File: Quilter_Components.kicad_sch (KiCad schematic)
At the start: 43 parts, among them J1 Conn_01x10_Male, J2 Conn_01x10_Male, J3 Conn_01x10_Male, J4 Eurorack_10_pin_power, U1 TL072, U2 TL074, U3 TL074, U4 TL074

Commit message: Added Readme and revision notes
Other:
- note added: "Potential V2 fixes: Mixed audio too loud - R6 try 4.7k in place of 10k (or variable resistor) Mixed audio has DC offset - use blocking caps on Audio_Out? Resonance cannot reach maximum on all variants - reduce Q Control resistor from 27k to 24-25k (R27, R40, R53, R66)"
- company: (none) -> Mountjoy Modular
- title: (none) -> Quilter Components
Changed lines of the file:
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@@
 (kicad_sch (version 20211123) (generator eeschema)
   (paper "A4")
+  (title_block
+    (title "Quilter Components")
+    (date "2023-03-22")
+    (rev "v1.0")
+    (company "Mountjoy Modular")
+  )
   (junction (at 66.04 167.64) (diameter 0) (color 0 0 0 0)
   )
@@
     (effects (font (size 3 3) (thickness 0.6) bold) (justify left bottom))
   )
+  (text "Potential V2 fixes:\nMixed audio too loud - R6 try 4.7k in place of 10k (or variable resistor)\nMixed audio has DC offset - use blocking caps on Audio_Out?\nResonance cannot reach maximum on all variants\n - reduce Q Control resistor from 27k to 24-25k (R27, R40, R53, R66)"
+    (at 204.47 179.07 0)
+    (effects (font (size 1.27 1.27)) (justify left bottom))
+  )
   (text "Interconnects and Test Points" (at 15.24 128.27 0)

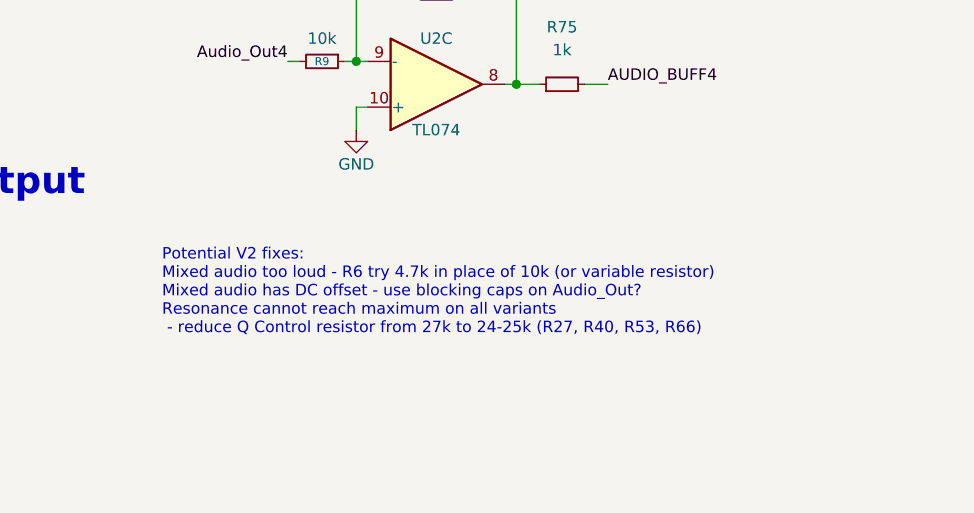
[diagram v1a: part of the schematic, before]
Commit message: Started adding DC blocking caps to audio outputs
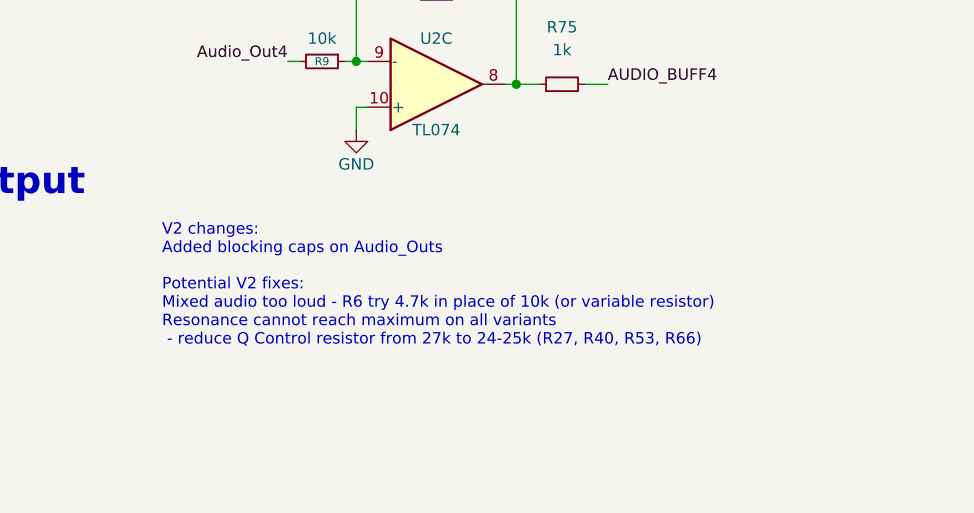
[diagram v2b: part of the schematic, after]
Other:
- note added: "Potential V2 fixes: Mixed audio too loud - R6 try 4.7k in place of 10k (or variable resistor) Resonance cannot reach maximum on all variants - reduce Q Control resistor from 27k to 24-25k (R27, R40, R53, R66)"
- note added: "V2 changes: Added blocking caps on Audio_Outs"
- note removed: "Potential V2 fixes: Mixed audio too loud - R6 try 4.7k in place of 10k (or variable resistor) Mixed audio has DC offset - use blocking caps on Audio_Out? Resonance cannot reach maximum on all variants - reduce Q Control resistor from 27k to 24-25k (R27, R40, R53, R66)"
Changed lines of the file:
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@@
     (effects (font (size 3 3) (thickness 0.6) bold) (justify left bottom))
+  )
+  (text "V2 changes:\nAdded blocking caps on Audio_Outs\n" (at 204.47 170.18 0)
+    (effects (font (size 1.27 1.27)) (justify left bottom))
   )
   (text "Output" (at 179.705 163.83 0)
     (effects (font (size 3 3) (thickness 0.6) bold) (justify left bottom))
   )
-  (text "Potential V2 fixes:\nMixed audio too loud - R6 try 4.7k in place of 10k (or variable resistor)\nMixed audio has DC offset - use blocking caps on Audio_Out?\nResonance cannot reach maximum on all variants\n - reduce Q Control resistor from 27k to 24-25k (R27, R40, R53, R66)"
-    (at 204.47 179.07 0)
+  (text "Potential V2 fixes:\nMixed audio too loud - R6 try 4.7k in place of 10k (or variable resistor)\nResonance cannot reach maximum on all variants\n - reduce Q Control resistor from 27k to 24-25k (R27, R40, R53, R66)"
+    (at 204.47 180.34 0)
     (effects (font (size 1.27 1.27)) (justify left bottom))
   )
@@
       (reference "C46") (unit 1) (value "1uF") (footprint "Capacitor_SMD:C_0603_1608Metric_Pad1.08x0.95mm_HandSolder")
     )
+    (path "/e84f8fd9-bd0a-4839-99bd-bd22e1164470/2c05cbd3-ef67-48b3-ba85-a3bd09df8735"
+      (reference "C47") (unit 1) (value "10uF") (footprint "Capacitor_SMD:C_0603_1608Metric_Pad1.08x0.95mm_HandSolder")
+    )
+    (path "/d9279b8b-eddd-468d-889c-ab682c020f45/2c05cbd3-ef67-48b3-ba85-a3bd09df8735"
+      (reference "C48") (unit 1) (value "10uF") (footprint "Capacitor_SMD:C_0603_1608Metric_Pad1.08x0.95mm_HandSolder")
+    )
+    (path "/3b233311-750f-4948-b3ee-a90810d15ca2/2c05cbd3-ef67-48b3-ba85-a3bd09df8735"
+      (reference "C49") (unit 1) (value "10uF") (footprint "Capacitor_SMD:C_0603_1608Metric_Pad1.08x0.95mm_HandSolder")
+    )
+    (path "/4ed2cc61-9552-41b0-be0f-c23455f3fe4c/2c05cbd3-ef67-48b3-ba85-a3bd09df8735"
+      (reference "C50") (unit 1) (value "10uF") (footprint "Capacitor_SMD:C_0603_1608Metric_Pad1.08x0.95mm_HandSolder")
+    )
     (path "/37b546d9-67b1-4476-930d-e62983801a78"

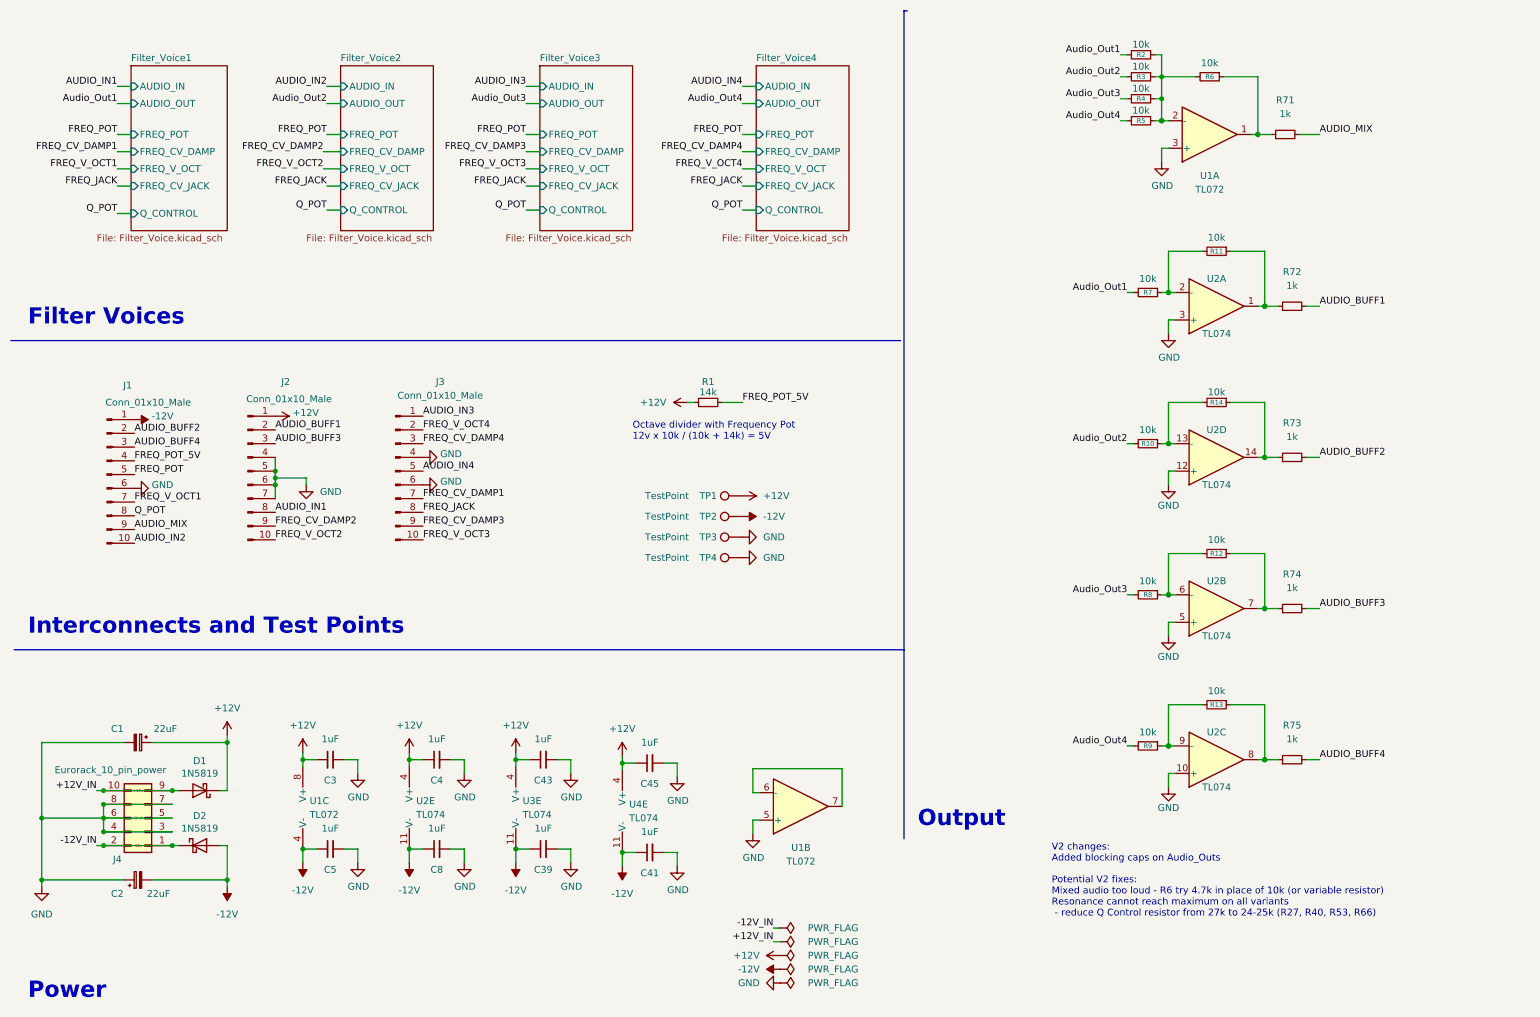
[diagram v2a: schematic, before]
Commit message: Updates for v2, including dc blocking caps on output
Also adjusted lower range of cutoff knob and tweaked various resistor values
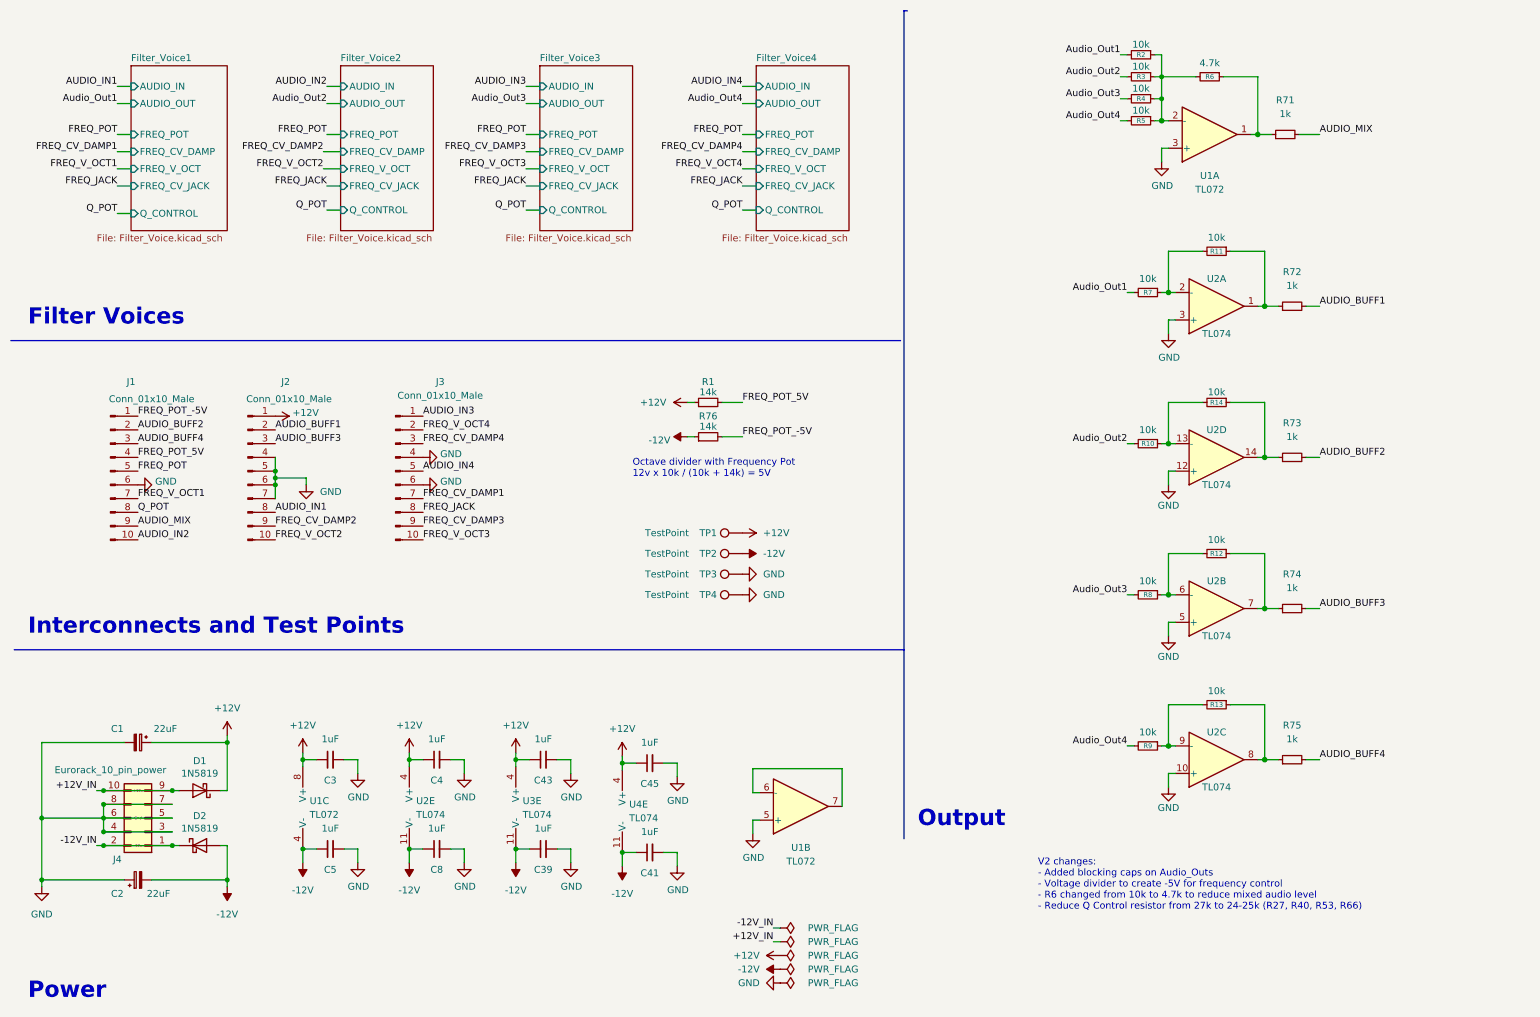
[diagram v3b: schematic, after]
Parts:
- added R76: 14k, Resistor_SMD:R_0603_1608Metric_Pad0.98x0.95mm_HandSolder, symbol Device:R_Small
- R6: value 10k -> 4.7k
- TP1, TP2, TP3, TP4: now left out of the parts list
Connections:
- net -12V: now also R76.1; no longer J1.1 (Pin_1)
- new net FREQ_POT_-5V: J1.1 (Pin_1), R76.2
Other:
- note added: "V2 changes: - Added blocking caps on Audio_Outs - Voltage divider to create -5V for frequency control - R6 changed from 10k to 4.7k to reduce mixed audio level - Reduce Q Control resistor from 27k to 24-25k (R27, R40, R53, R66)"
- note removed: "Potential V2 fixes: Mixed audio too loud - R6 try 4.7k in place of 10k (or variable resistor) Resonance cannot reach maximum on all variants - reduce Q Control resistor from 27k to 24-25k (R27, R40, R53, R66)"
- note removed: "V2 changes: Added blocking caps on Audio_Outs"
- moved on the sheet: J1, TP1, TP2, TP3, TP4

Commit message: Prepared v2 Controls and Components for manufacture
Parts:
- C1: Part_Number C134798 -> (none); Rotation 360 -> (none)
- C2: Part_Number C134793 -> (none); Rotation 270 -> (none)
- D1, D2: Part_Number C8598 -> (none)
- R10, R11, R12, R13, R14, R2, R3, R4, R5, R6, R7, R8, R9: Part_Number C25804 -> (none)
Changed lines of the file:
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@@
   )
   (symbol (lib_id "Connector:TestPoint") (at 147.32 116.84 90) (unit 1)
-    (in_bom no) (on_board no)
+    (in_bom no) (on_board yes)
     (property "Reference" "TP3" (id 0) (at 140.97 116.84 90))
     (property "Value" "TestPoint" (id 1) (at 133.35 116.84 90))
@@
       (effects (font (size 1.27 1.27)) hide)
     )
-    (property "Part_Number" "C134798" (id 4) (at 35.56 147.955 0)
-      (effects (font (size 1.27 1.27)) hide)
-    )
-    (property "Rotation" "360" (id 5) (at 35.56 147.955 0)
+    (property "Part_Number" "" (id 4) (at 35.56 147.955 0)
+      (effects (font (size 1.27 1.27)) hide)
+    )
+    (property "Rotation" "" (id 5) (at 35.56 147.955 0)
       (effects (font (size 1.27 1.27)) hide)
     )
@@
       (effects (font (size 1.27 1.27)) hide)
     )
-    (property "Part_Number" "C25804" (id 4) (at 220.98 28.956 0)
+    (property "Part_Number" "" (id 4) (at 220.98 28.956 0)
       (effects (font (size 1.27 1.27)) hide)
     )
@@
       (effects (font (size 1.27 1.27)) hide)
     )
-    (property "Datasheet" "https://datasheet.lcsc.com/szlcsc/Changjiang-Electronics-Tech-CJ-B5819W_C8598.pdf" (id 3) (at 46.99 156.845 0)
-      (effects (font (size 1.27 1.27)) hide)
-    )
-    (property "Part_Number" "C8598" (id 4) (at 46.99 156.845 0)
+    (property "Datasheet" "" (id 3) (at 46.99 156.845 0)
+      (effects (font (size 1.27 1.27)) hide)
+    )
+    (property "Part_Number" "" (id 4) (at 46.99 156.845 0)
       (effects (font (size 1.27 1.27)) hide)
     )
@@
       (effects (font (size 1.27 1.27)) hide)
     )
-    (property "Part_Number" "C25804" (id 4) (at 220.98 24.892 0)
+    (property "Part_Number" "" (id 4) (at 220.98 24.892 0)
       (effects (font (size 1.27 1.27)) hide)
     )
@@
       (effects (font (size 1.27 1.27)) hide)
     )
-    (property "Part_Number" "C25804" (id 4) (at 220.98 20.828 0)
+    (property "Part_Number" "" (id 4) (at 220.98 20.828 0)
       (effects (font (size 1.27 1.27)) hide)
     )
@@
       (effects (font (size 1.27 1.27)) hide)
     )
-    (property "Part_Number" "C25804" (id 4) (at 222.25 148.59 0)
+    (property "Part_Number" "" (id 4) (at 222.25 148.59 0)
       (effects (font (size 1.27 1.27)) hide)
     )
@@
       (effects (font (size 1.27 1.27)) hide)
     )
-    (property "Part_Number" "C25804" (id 4) (at 234.95 57.15 0)
+    (property "Part_Number" "" (id 4) (at 234.95 57.15 0)
       (effects (font (size 1.27 1.27)) hide)
     )
@@
       (effects (font (size 1.27 1.27)) hide)
     )
-    (property "Part_Number" "C25804" (id 4) (at 220.98 33.02 0)
+    (property "Part_Number" "" (id 4) (at 220.98 33.02 0)
       (effects (font (size 1.27 1.27)) hide)
     )
@@
   )
   (symbol (lib_id "Connector:TestPoint") (at 147.32 113.03 90) (unit 1)
-    (in_bom no) (on_board no)
+    (in_bom no) (on_board yes)
     (property "Reference" "TP2" (id 0) (at 140.97 113.03 90))
     (property "Value" "TestPoint" (id 1) (at 133.35 113.03 90))
@@
       (effects (font (size 1.27 1.27)) hide)
     )
-    (property "Datasheet" "https://datasheet.lcsc.com/szlcsc/Changjiang-Electronics-Tech-CJ-B5819W_C8598.pdf" (id 3) (at 46.99 167.005 0)
-      (effects (font (size 1.27 1.27)) hide)
-    )
-    (property "Part_Number" "C8598" (id 4) (at 46.99 167.005 0)
+    (property "Datasheet" "" (id 3) (at 46.99 167.005 0)
+      (effects (font (size 1.27 1.27)) hide)
+    )
+    (property "Part_Number" "" (id 4) (at 46.99 167.005 0)
       (effects (font (size 1.27 1.27)) hide)
     )
@@
       (effects (font (size 1.27 1.27)) hide)
     )
-    (property "Part_Number" "C25804" (id 4) (at 222.25 120.65 0)
+    (property "Part_Number" "" (id 4) (at 222.25 120.65 0)
       (effects (font (size 1.27 1.27)) hide)
     )
@@
       (effects (font (size 1.27 1.27)) hide)
     )
-    (property "Part_Number" "C25804" (id 4) (at 222.25 92.71 0)
+    (property "Part_Number" "" (id 4) (at 222.25 92.71 0)
       (effects (font (size 1.27 1.27)) hide)
     )
@@
       (effects (font (size 1.27 1.27)) hide)
     )
-    (property "Part_Number" "C25804" (id 4) (at 234.95 140.97 0)
+    (property "Part_Number" "" (id 4) (at 234.95 140.97 0)
       (effects (font (size 1.27 1.27)) hide)
     )
@@
       (effects (font (size 1.27 1.27)) hide)
     )
-    (property "Part_Number" "C25804" (id 4) (at 222.25 64.77 0)
+    (property "Part_Number" "" (id 4) (at 222.25 64.77 0)
       (effects (font (size 1.27 1.27)) hide)
     )
@@
       (effects (font (size 1.27 1.27)) hide)
     )
-    (property "Part_Number" "C25804" (id 4) (at 234.95 85.09 0)
+    (property "Part_Number" "" (id 4) (at 234.95 85.09 0)
       (effects (font (size 1.27 1.27)) hide)
     )
@@
       (effects (font (size 1.27 1.27)) hide)
     )
-    (property "Part_Number" "C25804" (id 4) (at 234.95 113.03 0)
+    (property "Part_Number" "" (id 4) (at 234.95 113.03 0)
       (effects (font (size 1.27 1.27)) hide)
     )
@@
   )
   (symbol (lib_id "Connector:TestPoint") (at 147.32 109.22 90) (unit 1)
-    (in_bom no) (on_board no)
+    (in_bom no) (on_board yes)
     (property "Reference" "TP1" (id 0) (at 140.97 109.22 90))
     (property "Value" "TestPoint" (id 1) (at 133.35 109.22 90))
@@
       (effects (font (size 1.27 1.27)) hide)
     )
-    (property "Part_Number" "C134793" (id 4) (at 35.56 173.355 0)
-      (effects (font (size 1.27 1.27)) hide)
-    )
-    (property "Rotation" "270" (id 5) (at 35.56 173.355 0)
+    (property "Part_Number" "" (id 4) (at 35.56 173.355 0)
+      (effects (font (size 1.27 1.27)) hide)
+    )
+    (property "Rotation" "" (id 5) (at 35.56 173.355 0)
       (effects (font (size 1.27 1.27)) hide)
     )
@@
       (effects (font (size 1.27 1.27)) hide)
     )
-    (property "Part_Number" "C25804" (id 4) (at 233.68 24.892 0)
+    (property "Part_Number" "" (id 4) (at 233.68 24.892 0)
       (effects (font (size 1.27 1.27)) hide)
     )
@@
   )
   (symbol (lib_id "Connector:TestPoint") (at 147.32 120.65 90) (unit 1)
-    (in_bom no) (on_board no)
+    (in_bom no) (on_board yes)
     (property "Reference" "TP4" (id 0) (at 140.97 120.65 90))
     (property "Value" "TestPoint" (id 1) (at 133.35 120.65 90))
@@
     )
     (path "/e84f8fd9-bd0a-4839-99bd-bd22e1164470/d818ee47-d9e1-4bdb-83a6-ea087505d6aa"
-      (reference "C11") (unit 1) (value "10nF_C0G") (footprint "Capacitor_SMD:C_0603_1608Metric_Pad1.08x0.95mm_HandSolder")
+      (reference "C11") (unit 1) (value "10nF") (footprint "Capacitor_SMD:C_0603_1608Metric_Pad1.08x0.95mm_HandSolder")
     )
     (path "/e84f8fd9-bd0a-4839-99bd-bd22e1164470/0da5ff5b-c986-4f91-afa9-a315f9dec90d"
@@
     )
     (path "/d9279b8b-eddd-468d-889c-ab682c020f45/d818ee47-d9e1-4bdb-83a6-ea087505d6aa"
-      (reference "C19") (unit 1) (value "10nF_C0G") (footprint "Capacitor_SMD:C_0603_1608Metric_Pad1.08x0.95mm_HandSolder")
+      (reference "C19") (unit 1) (value "10nF") (footprint "Capacitor_SMD:C_0603_1608Metric_Pad1.08x0.95mm_HandSolder")
     )
     (path "/d9279b8b-eddd-468d-889c-ab682c020f45/0da5ff5b-c986-4f91-afa9-a315f9dec90d"
@@
     )
     (path "/3b233311-750f-4948-b3ee-a90810d15ca2/d818ee47-d9e1-4bdb-83a6-ea087505d6aa"
-      (reference "C27") (unit 1) (value "10nF_C0G") (footprint "Capacitor_SMD:C_0603_1608Metric_Pad1.08x0.95mm_HandSolder")
+      (reference "C27") (unit 1) (value "10nF") (footprint "Capacitor_SMD:C_0603_1608Metric_Pad1.08x0.95mm_HandSolder")
     )
     (path "/3b233311-750f-4948-b3ee-a90810d15ca2/0da5ff5b-c986-4f91-afa9-a315f9dec90d"
@@
     )
     (path "/4ed2cc61-9552-41b0-be0f-c23455f3fe4c/d818ee47-d9e1-4bdb-83a6-ea087505d6aa"
-      (reference "C35") (unit 1) (value "10nF_C0G") (footprint "Capacitor_SMD:C_0603_1608Metric_Pad1.08x0.95mm_HandSolder")
+      (reference "C35") (unit 1) (value "10nF") (footprint "Capacitor_SMD:C_0603_1608Metric_Pad1.08x0.95mm_HandSolder")
     )
     (path "/4ed2cc61-9552-41b0-be0f-c23455f3fe4c/0da5ff5b-c986-4f91-afa9-a315f9dec90d"
